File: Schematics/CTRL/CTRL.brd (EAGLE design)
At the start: 328.9 x 291.8 mm, 48 parts

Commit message: LDO
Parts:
- added OCP: (no value), pinhead:1X01
- added V5: 7410N, 74ttl-din:DIL14
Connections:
- new net N$6: V5.13, V5.6
- new net OCP: OCP.1, V5.12
- net CLK: now also V5.2
- net GND: now also V5.7
- net OUA: now also V5.5
- net OUX: now also V5.3
- net OUY: now also V5.4
- net T2: now also V5.1
- net VCC: now also V5.14
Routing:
- net OUY: track 115.7 -> 167.7 mm
- net OUX: track 115.7 -> 167.7 mm
- net OUA: track 181.0 -> 226.7 mm
- net CLK: track 784.6 -> 826.9 mm, vias 7 -> 10
- net VCC: track 968.0 -> 1007.2 mm
- net T2: track 699.8 -> 734.4 mm, vias 8 -> 9
- net GND: track 970.0 -> 995.9 mm
- net N$6: track 0.00 -> 16.3 mm
- net OCP: track 0.00 -> 5.61 mm
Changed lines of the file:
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@@
 <drawing>
 <settings>
-<setting alwaysvectorfont="yes"/>
+<setting alwaysvectorfont="no"/>
 <setting verticaltext="up"/>
 </settings>
@@
 <dimension x1="193.04" y1="138.43" x2="193.04" y2="67.31" x3="344.17" y3="102.87" textsize="1.778" layer="20"/>
 <dimension x1="96.52" y1="208.28" x2="55.88" y2="208.28" x3="76.2" y3="275.59" textsize="1.778" layer="20"/>
+<dimension x1="324.612" y1="215.9" x2="324.612" y2="289.306" x3="347.98" y3="252.603" textsize="1.778" layer="20"/>
 </plain>
 <attributes>
@@
 <attribute name="VALUE" x="138.43" y="64.135" size="1.27" layer="27"/>
 </element>
+<element name="V5" library="74ttl-din" library_urn="urn:adsk.eagle:library:84" package="DIL14" package3d_urn="urn:adsk.eagle:package:16407/2" value="7410N" x="255.27" y="158.75" smashed="yes" rot="R180">
+<attribute name="NAME" x="264.541" y="161.798" size="1.27" layer="25" ratio="10" rot="R270"/>
+<attribute name="POPULARITY" value="0" x="255.27" y="158.75" size="1.778" layer="27" rot="R180" display="off"/>
+<attribute name="VALUE" x="262.001" y="159.385" size="1.27" layer="27" ratio="10" rot="R180"/>
+</element>
+<element name="OCP" library="pinhead" library_urn="urn:adsk.eagle:library:325" package="1X01" package3d_urn="urn:adsk.eagle:package:22485/2" value="" x="260.35" y="151.13" smashed="yes">
+<attribute name="NAME" x="259.0038" y="152.9588" size="1.27" layer="25" ratio="10"/>
+<attribute name="POPULARITY" value="64" x="260.35" y="151.13" size="1.778" layer="27" display="off"/>
+<attribute name="VALUE" x="259.08" y="147.955" size="1.27" layer="27"/>
+</element>
 </elements>
 <signals>
@@
 <wire x1="283.21" y1="171.45" x2="283.21" y2="172.72" width="0.4" layer="1"/>
 <wire x1="283.21" y1="172.72" x2="273.812" y2="182.118" width="0.4" layer="1"/>
-<wire x1="257.2904" y1="182.118" x2="257.2706" y2="182.1378" width="0.4" layer="1"/>
-<via x="257.2706" y="182.1378" extent="1-16" drill="0.35"/>
-<wire x1="257.2706" y1="182.1378" x2="255.8094" y2="182.1378" width="0.4" layer="16"/>
-<via x="255.8094" y="182.1378" extent="1-16" drill="0.35"/>
-<wire x1="255.8094" y1="182.1378" x2="220.5478" y2="182.1378" width="0.4" layer="1"/>
+<wire x1="258.5604" y1="182.118" x2="258.5406" y2="182.1378" width="0.4" layer="1"/>
+<via x="258.5406" y="182.1378" extent="1-16" drill="0.35"/>
+<wire x1="258.5406" y1="182.1378" x2="254.5394" y2="182.1378" width="0.4" layer="16"/>
+<via x="254.5394" y="182.1378" extent="1-16" drill="0.35"/>
+<wire x1="254.5394" y1="182.1378" x2="220.5478" y2="182.1378" width="0.4" layer="1"/>
 <wire x1="220.5478" y1="182.1378" x2="220.4406" y2="182.245" width="0.4" layer="1"/>
 <via x="220.4406" y="182.245" extent="1-16" drill="0.35"/>
@@
 <wire x1="194.31" y1="147.32" x2="190.5" y2="143.51" width="0.4" layer="16"/>
 <wire x1="190.5" y1="143.51" x2="190.5" y2="138.43" width="0.4" layer="16"/>
-<wire x1="273.812" y1="182.118" x2="257.2904" y2="182.118" width="0.4" layer="1"/>
+<wire x1="273.812" y1="182.118" x2="258.5604" y2="182.118" width="0.4" layer="1"/>
 <wire x1="194.31" y1="182.245" x2="194.31" y2="147.32" width="0.4" layer="16"/>
 <wire x1="194.31" y1="182.245" x2="122.555" y2="182.245" width="0.4" layer="1"/>
@@
 <wire x1="122.555" y1="182.245" x2="53.34" y2="113.03" width="0.4" layer="1"/>
 <wire x1="53.34" y1="113.03" x2="53.34" y2="83.82" width="0.4" layer="1"/>
+<wire x1="258.5406" y1="182.1378" x2="254.5394" y2="182.1378" width="0" layer="19"/>
 </signal>
 <signal name="LDY">
@@
 <wire x1="224.79" y1="177.8" x2="224.79" y2="194.31" width="0.4" layer="16"/>
 <wire x1="224.79" y1="194.31" x2="240.03" y2="209.55" width="0.4" layer="16"/>
+<contactref element="V5" pad="3"/>
+<wire x1="273.05" y1="208.28" x2="273.05" y2="205.74" width="0.4" layer="16"/>
+<wire x1="273.05" y1="205.74" x2="261.62" y2="194.31" width="0.4" layer="16"/>
+<wire x1="261.62" y1="194.31" x2="261.62" y2="173.99" width="0.4" layer="16"/>
+<wire x1="257.81" y1="170.18" x2="261.62" y2="173.99" width="0.4" layer="16"/>
+<wire x1="257.81" y1="162.56" x2="257.81" y2="170.18" width="0.4" layer="16"/>
 </signal>
 <signal name="OUY">
@@
 <wire x1="223.52" y1="194.31" x2="240.03" y2="210.82" width="0.4" layer="16"/>
 <wire x1="240.03" y1="210.82" x2="269.24" y2="210.82" width="0.4" layer="16"/>
+<contactref element="V5" pad="4"/>
+<wire x1="255.27" y1="162.56" x2="255.27" y2="170.18" width="0.4" layer="16"/>
+<wire x1="260.35" y1="195.58" x2="270.51" y2="205.74" width="0.4" layer="16"/>
+<wire x1="270.51" y1="205.74" x2="270.51" y2="208.28" width="0.4" layer="16"/>
+<wire x1="255.27" y1="170.18" x2="260.35" y2="175.26" width="0.4" layer="16"/>
+<wire x1="260.35" y1="175.26" x2="260.35" y2="195.58" width="0.4" layer="16"/>
 </signal>
 <signal name="OUA">
@@
 <wire x1="217.17" y1="135.89" x2="210.82" y2="129.54" width="0.4" layer="16"/>
 <wire x1="210.82" y1="129.54" x2="210.82" y2="67.31" width="0.4" layer="16"/>
-<wire x1="267.97" y1="208.28" x2="240.03" y2="208.28" width="0.4" layer="16"/>
+<wire x1="267.97" y1="208.28" x2="252.73" y2="208.28" width="0.4" layer="16"/>
+<wire x1="252.73" y1="208.28" x2="240.03" y2="208.28" width="0.4" layer="16"/>
 <wire x1="240.03" y1="208.28" x2="226.06" y2="194.31" width="0.4" layer="16"/>
 <wire x1="226.06" y1="194.31" x2="226.06" y2="176.53" width="0.4" layer="16"/>
 <wire x1="226.06" y1="176.53" x2="222.25" y2="172.72" width="0.4" layer="16"/>
 <wire x1="217.17" y1="153.67" x2="217.17" y2="135.89" width="0.4" layer="16"/>
+<contactref element="V5" pad="5"/>
+<wire x1="252.73" y1="162.56" x2="252.73" y2="208.28" width="0.4" layer="16"/>
 </signal>
 <signal name="0XFF">
@@
 <wire x1="311.15" y1="229.87" x2="316.23" y2="229.87" width="0.4" layer="1"/>
 <wire x1="316.23" y1="229.87" x2="324.612" y2="229.87" width="0.4" layer="1"/>
+<contactref element="V5" pad="14"/>
+<wire x1="262.89" y1="154.94" x2="262.89" y2="146.05" width="0.4" layer="16"/>
+<wire x1="260.35" y1="143.51" x2="233.68" y2="143.51" width="0.4" layer="16"/>
+<wire x1="262.89" y1="146.05" x2="260.35" y2="143.51" width="0.4" layer="16"/>
 </signal>
 <signal name="GND">
@@
 <wire x1="49.53" y1="10.16" x2="24.13" y2="35.56" width="0.4" layer="1"/>
 <wire x1="24.13" y1="35.56" x2="24.13" y2="212.09" width="0.4" layer="1"/>
+<contactref element="V5" pad="7"/>
+<wire x1="231.14" y1="143.51" x2="231.14" y2="146.05" width="0.4" layer="16"/>
+<wire x1="231.14" y1="146.05" x2="247.65" y2="162.56" width="0.4" layer="16"/>
 </signal>
 <signal name="0X00">
@@
 <wire x1="322.961" y1="181.991" x2="322.961" y2="131.191" width="0.4" layer="1"/>
 <wire x1="257.81" y1="105.41" x2="257.81" y2="120.65" width="0.4" layer="1"/>
+<contactref element="V5" pad="1"/>
+<wire x1="262.89" y1="162.56" x2="266.7" y2="158.75" width="0.4" layer="16"/>
+<wire x1="266.7" y1="158.75" x2="266.7" y2="135.89" width="0.4" layer="16"/>
+<via x="266.7" y="135.89" extent="1-16" drill="0.35"/>
+<wire x1="266.7" y1="135.89" x2="266.7" y2="129.54" width="0.4" layer="1"/>
 </signal>
 <signal name="T3">
@@
 <via x="236.22" y="125.73" extent="1-16" drill="0.35"/>
 <wire x1="236.22" y1="125.73" x2="236.22" y2="138.43" width="0.4" layer="16"/>
+<contactref element="V5" pad="2"/>
+<wire x1="260.35" y1="162.56" x2="260.35" y2="160.02" width="0.4" layer="16"/>
+<wire x1="260.35" y1="160.02" x2="259.08" y2="158.75" width="0.4" layer="16"/>
+<wire x1="259.08" y1="158.75" x2="252.73" y2="158.75" width="0.4" layer="16"/>
+<via x="252.73" y="158.75" extent="1-16" drill="0.35"/>
+<wire x1="252.73" y1="158.75" x2="245.11" y2="158.75" width="0.4" layer="1"/>
+<wire x1="245.11" y1="158.75" x2="237.49" y2="151.13" width="0.4" layer="1"/>
+<wire x1="237.49" y1="151.13" x2="237.49" y2="149.86" width="0.4" layer="1"/>
+<via x="237.49" y="149.86" extent="1-16" drill="0.35"/>
+<wire x1="237.49" y1="149.86" x2="237.49" y2="144.78" width="0.4" layer="16"/>
+<via x="237.49" y="144.78" extent="1-16" drill="0.35"/>
+<wire x1="237.49" y1="144.78" x2="237.49" y2="139.7" width="0.4" layer="1"/>
+<wire x1="237.49" y1="139.7" x2="236.22" y2="138.43" width="0.4" layer="1"/>
 </signal>
 <signal name="N$1">
@@
 <wire x1="295.91" y1="78.74" x2="295.91" y2="90.17" width="0.4" layer="16"/>
 </signal>
+<signal name="OCP">
+<contactref element="V5" pad="12"/>
+<contactref element="OCP" pad="1"/>
+<wire x1="260.35" y1="151.13" x2="259.08" y2="151.13" width="0.4" layer="1"/>
+<wire x1="259.08" y1="151.13" x2="257.81" y2="152.4" width="0.4" layer="1"/>
+<wire x1="257.81" y1="152.4" x2="257.81" y2="154.94" width="0.4" layer="1"/>
+</signal>
+<signal name="N$6">
+<contactref element="V5" pad="6"/>
+<contactref element="V5" pad="13"/>
+<wire x1="260.35" y1="154.94" x2="260.35" y2="156.21" width="0.4" layer="16"/>
+<wire x1="260.35" y1="156.21" x2="259.715" y2="156.845" width="0.4" layer="16"/>
+<wire x1="252.095" y1="156.845" x2="250.19" y2="158.75" width="0.4" layer="16"/>
+<wire x1="250.19" y1="158.75" x2="250.19" y2="162.56" width="0.4" layer="16"/>
+<wire x1="259.715" y1="156.845" x2="252.095" y2="156.845" width="0.4" layer="16"/>
+</signal>
 </signals>

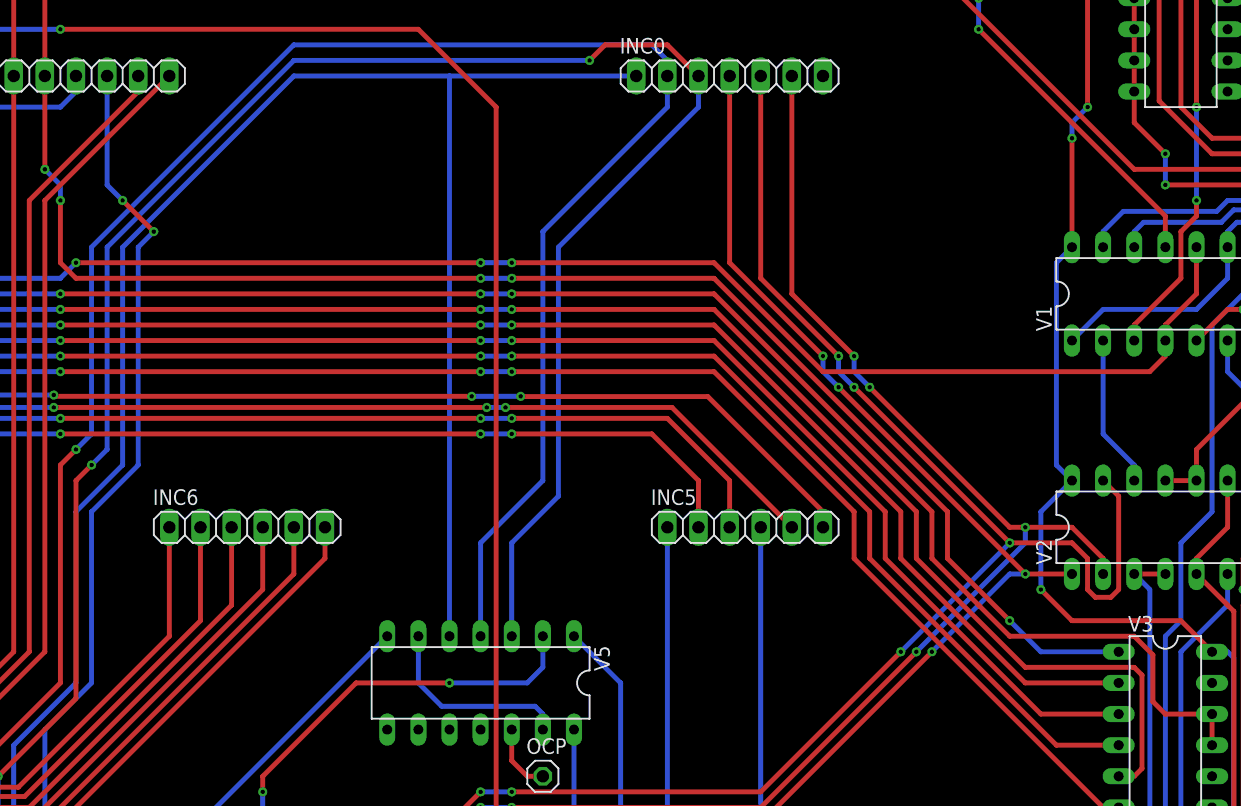
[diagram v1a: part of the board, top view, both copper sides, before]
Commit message: Fixed problem with 0xXX
RET wasnt negated, 0xFF and 0xFE started to over heat when T2 was High.
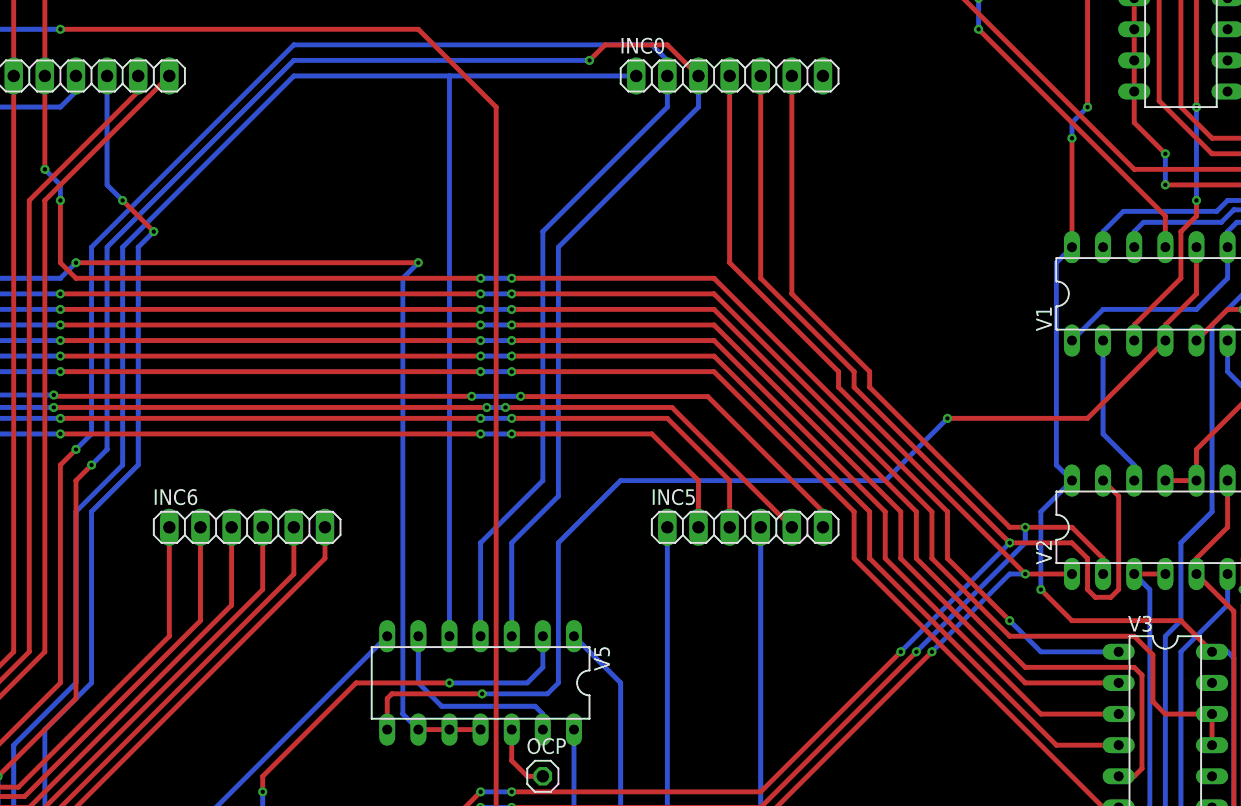
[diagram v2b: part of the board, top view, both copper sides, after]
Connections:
- new net L1: V1.10, V1.4, V5.8
- net RET: now also V5.10, V5.11, V5.9; no longer V1.10, V1.4
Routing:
- net L1: track 0.00 -> 93.5 mm, vias 0 -> 2
- net RET: track 578.1 -> 547.2 mm, vias 11 -> 10
- net CLY: vias 6 -> 4
- net CLX: vias 6 -> 4
- net CLA: vias 6 -> 4
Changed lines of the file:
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@@
 <signal name="RET">
 <contactref element="INC2" pad="2"/>
-<contactref element="V1" pad="10"/>
-<contactref element="V1" pad="4"/>
 <contactref element="RAM-OP" pad="6"/>
 <contactref element="PC-OP0" pad="13"/>
@@
 <wire x1="220.98" y1="191.77" x2="222.25" y2="193.04" width="0.4" layer="16"/>
 <via x="222.25" y="193.04" extent="1-16" drill="0.35"/>
-<wire x1="222.25" y1="193.04" x2="255.27" y2="193.04" width="0.4" layer="1"/>
-<via x="255.27" y="193.04" extent="1-16" drill="0.35"/>
-<wire x1="255.27" y1="193.04" x2="257.81" y2="193.04" width="0.4" layer="16"/>
-<via x="257.81" y="193.04" extent="1-16" drill="0.35"/>
-<wire x1="257.81" y1="193.04" x2="274.32" y2="193.04" width="0.4" layer="1"/>
-<wire x1="283.21" y1="184.15" x2="309.88" y2="184.15" width="0.4" layer="1"/>
-<wire x1="309.88" y1="184.15" x2="311.15" y2="185.42" width="0.4" layer="1"/>
-<wire x1="311.15" y1="185.42" x2="311.15" y2="186.69" width="0.4" layer="1"/>
-<wire x1="274.32" y1="193.04" x2="283.21" y2="184.15" width="0.4" layer="1"/>
-<wire x1="311.15" y1="186.69" x2="311.15" y2="187.96" width="0.4" layer="1"/>
-<wire x1="311.15" y1="187.96" x2="313.69" y2="190.5" width="0.4" layer="1"/>
-<wire x1="313.69" y1="190.5" x2="313.69" y2="194.31" width="0.4" layer="1"/>
+<wire x1="222.25" y1="193.04" x2="250.19" y2="193.04" width="0.4" layer="1"/>
+<contactref element="V5" pad="10"/>
+<contactref element="V5" pad="11"/>
+<contactref element="V5" pad="9"/>
+<wire x1="250.19" y1="154.94" x2="252.73" y2="154.94" width="0.4" layer="1"/>
+<wire x1="252.73" y1="154.94" x2="255.27" y2="154.94" width="0.4" layer="1"/>
+<wire x1="250.19" y1="154.94" x2="248.92" y2="156.21" width="0.4" layer="16"/>
+<wire x1="248.92" y1="191.77" x2="250.19" y2="193.04" width="0.4" layer="16"/>
+<via x="250.19" y="193.04" extent="1-16" drill="0.35"/>
+<wire x1="248.92" y1="156.21" x2="248.92" y2="191.77" width="0.4" layer="16"/>
 </signal>
 <signal name="HLT">
@@
 <contactref element="REG-OP" pad="30"/>
 <wire x1="306.07" y1="167.64" x2="306.07" y2="168.91" width="0.4" layer="1"/>
-<via x="287.02" y="182.88" extent="1-16" drill="0.35"/>
-<wire x1="287.02" y1="182.88" x2="285.75" y2="184.15" width="0.4" layer="16"/>
-<wire x1="285.75" y1="184.15" x2="285.75" y2="185.42" width="0.4" layer="16"/>
-<via x="285.75" y="185.42" extent="1-16" drill="0.35"/>
-<wire x1="285.75" y1="185.42" x2="280.67" y2="190.5" width="0.4" layer="1"/>
 <wire x1="306.07" y1="168.91" x2="303.53" y2="171.45" width="0.4" layer="1"/>
 <wire x1="303.53" y1="171.45" x2="299.72" y2="171.45" width="0.4" layer="1"/>
 <wire x1="299.72" y1="171.45" x2="298.45" y2="171.45" width="0.4" layer="1"/>
-<wire x1="298.45" y1="171.45" x2="287.02" y2="182.88" width="0.4" layer="1"/>
-<wire x1="280.67" y1="190.5" x2="280.67" y2="208.28" width="0.4" layer="1"/>
+<wire x1="287.02" y1="182.88" x2="298.45" y2="171.45" width="0.4" layer="1"/>
+<wire x1="280.67" y1="208.28" x2="280.67" y2="190.5" width="0.4" layer="1"/>
 <wire x1="254" y1="147.32" x2="255.27" y2="148.59" width="0.4" layer="1"/>
 <via x="255.27" y="148.59" extent="1-16" drill="0.35"/>
@@
 <wire x1="220.98" y1="140.335" x2="227.965" y2="147.32" width="0.4" layer="1"/>
 <wire x1="227.965" y1="147.32" x2="254" y2="147.32" width="0.4" layer="1"/>
+<wire x1="287.02" y1="184.15" x2="287.02" y2="182.88" width="0.4" layer="1"/>
+<wire x1="280.67" y1="190.5" x2="287.02" y2="184.15" width="0.4" layer="1"/>
 </signal>
 <signal name="CLY">
@@
 <contactref element="V2" pad="13"/>
 <contactref element="REG-OP" pad="29"/>
-<wire x1="278.13" y1="191.77" x2="284.48" y2="185.42" width="0.4" layer="1"/>
-<via x="284.48" y="185.42" extent="1-16" drill="0.35"/>
-<wire x1="284.48" y1="185.42" x2="284.48" y2="184.15" width="0.4" layer="16"/>
-<wire x1="284.48" y1="184.15" x2="285.75" y2="182.88" width="0.4" layer="16"/>
-<via x="285.75" y="182.88" extent="1-16" drill="0.35"/>
 <wire x1="285.75" y1="182.88" x2="298.45" y2="170.18" width="0.4" layer="1"/>
 <wire x1="298.45" y1="170.18" x2="303.53" y2="170.18" width="0.4" layer="1"/>
@@
 <via x="298.45" y="170.18" extent="1-16" drill="0.35"/>
 <wire x1="226.949" y1="148.209" x2="253.619" y2="148.209" width="0.4" layer="1"/>
+<wire x1="285.75" y1="184.15" x2="285.75" y2="182.88" width="0.4" layer="1"/>
+<wire x1="278.13" y1="191.77" x2="285.75" y2="184.15" width="0.4" layer="1"/>
 </signal>
 <signal name="CLA">
@@
 <contactref element="ALU-OP0" pad="30"/>
 <wire x1="303.53" y1="167.64" x2="299.72" y2="167.64" width="0.4" layer="1"/>
-<via x="284.48" y="182.88" extent="1-16" drill="0.35"/>
-<wire x1="284.48" y1="182.88" x2="283.21" y2="184.15" width="0.4" layer="16"/>
-<wire x1="283.21" y1="184.15" x2="283.21" y2="185.42" width="0.4" layer="16"/>
-<via x="283.21" y="185.42" extent="1-16" drill="0.35"/>
-<wire x1="283.21" y1="185.42" x2="275.59" y2="193.04" width="0.4" layer="1"/>
-<wire x1="275.59" y1="193.04" x2="275.59" y2="208.28" width="0.4" layer="1"/>
-<wire x1="299.72" y1="167.64" x2="284.48" y2="182.88" width="0.4" layer="1"/>
+<wire x1="275.59" y1="208.28" x2="275.59" y2="193.04" width="0.4" layer="1"/>
+<wire x1="284.48" y1="182.88" x2="299.72" y2="167.64" width="0.4" layer="1"/>
 <wire x1="213.36" y1="67.31" x2="213.36" y2="127" width="0.4" layer="1"/>
 <wire x1="213.36" y1="127" x2="222.25" y2="135.89" width="0.4" layer="1"/>
@@
 <via x="299.72" y="167.64" extent="1-16" drill="0.35"/>
 <wire x1="228.6" y1="146.05" x2="254" y2="146.05" width="0.4" layer="1"/>
+<wire x1="284.48" y1="184.15" x2="284.48" y2="182.88" width="0.4" layer="1"/>
+<wire x1="275.59" y1="193.04" x2="284.48" y2="184.15" width="0.4" layer="1"/>
 </signal>
 <signal name="OUX">
@@
 <wire x1="259.715" y1="156.845" x2="252.095" y2="156.845" width="0.4" layer="16"/>
 </signal>
+<signal name="L1">
+<contactref element="V5" pad="8"/>
+<contactref element="V1" pad="4"/>
+<wire x1="311.15" y1="186.69" x2="311.15" y2="187.96" width="0.4" layer="1"/>
+<wire x1="311.15" y1="187.96" x2="313.69" y2="190.5" width="0.4" layer="1"/>
+<contactref element="V1" pad="10"/>
+<wire x1="313.69" y1="190.5" x2="313.69" y2="194.31" width="0.4" layer="1"/>
+<wire x1="311.15" y1="186.69" x2="304.8" y2="180.34" width="0.4" layer="1"/>
+<wire x1="304.8" y1="180.34" x2="293.37" y2="180.34" width="0.4" layer="1"/>
+<via x="293.37" y="180.34" extent="1-16" drill="0.35"/>
+<wire x1="293.37" y1="180.34" x2="288.29" y2="175.26" width="0.4" layer="16"/>
+<wire x1="288.29" y1="175.26" x2="266.7" y2="175.26" width="0.4" layer="16"/>
+<wire x1="266.7" y1="175.26" x2="261.62" y2="170.18" width="0.4" layer="16"/>
+<wire x1="261.62" y1="170.18" x2="261.62" y2="158.75" width="0.4" layer="16"/>
+<wire x1="261.62" y1="158.75" x2="260.731" y2="157.861" width="0.4" layer="16"/>
+<wire x1="260.731" y1="157.861" x2="255.397" y2="157.861" width="0.4" layer="16"/>
+<via x="255.397" y="157.861" extent="1-16" drill="0.35"/>
+<wire x1="255.397" y1="157.861" x2="248.031" y2="157.861" width="0.4" layer="1"/>
+<wire x1="248.031" y1="157.861" x2="247.65" y2="157.48" width="0.4" layer="1"/>
+<wire x1="247.65" y1="157.48" x2="247.65" y2="154.94" width="0.4" layer="1"/>
+</signal>
 </signals>
